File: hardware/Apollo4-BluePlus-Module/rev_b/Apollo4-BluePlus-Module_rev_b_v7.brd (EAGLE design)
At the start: 13 x 20 mm, 102 parts, among them J1 TC2030-JLINK-NL-2SIDE, J2 TC2030-JLINK-NL-2SIDE, P1 CASTELLATION4L, P10 CASTELLATION4L, P11 CASTELLATION4L, P12 CASTELLATION4L, P13 CASTELLATION4L, P14 CASTELLATION4L, P15 CASTELLATION4L, P18 CASTELLATION4L, P19 CASTELLATION4L, P2 CASTELLATION4L, P20 CASTELLATION4L, P21 CASTELLATION4L, P22 CASTELLATION4L, P23 CASTELLATION4L, P24 CASTELLATION4L, P25 CASTELLATION4L, P26 CASTELLATION4L, P27 CASTELLATION4L, P28 CASTELLATION4L, P29 CASTELLATION4L, P3 CASTELLATION4L, P30 CASTELLATION4L, P31 CASTELLATION4L, P32 CASTELLATION4L, P33 CASTELLATION4L, P34 CASTELLATION4L, P35 CASTELLATION4L, P36 CASTELLATION4L, P37 CASTELLATION4L, P38 CASTELLATION4L, P39 CASTELLATION4L, P4 CASTELLATION4L, P40 CASTELLATION4L, P41 CASTELLATION4L, P42 CASTELLATION4L, P43 CASTELLATION4L, P44 CASTELLATION4L, P45 CASTELLATION4L, P46 CASTELLATION4L, P47 CASTELLATION4L, P48 CASTELLATION4L, P5 CASTELLATION4L, P6 CASTELLATION4L, P7 CASTELLATION4L, P8 CASTELLATION4L, P9 CASTELLATION4L, U1 APOLLO4_BLUE_PLUS_SOC_KBR, X1 TXC-9HT12, X2 ABM12W

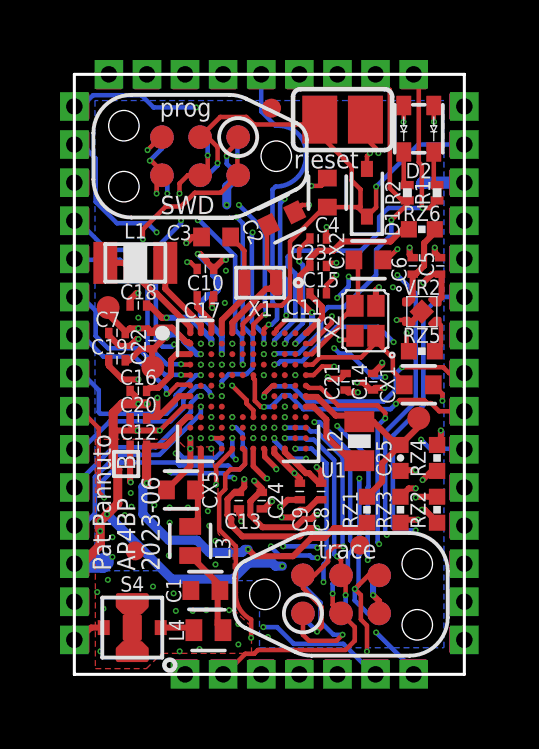
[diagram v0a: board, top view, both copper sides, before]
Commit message: ap4bp-mod-rev_b: remove RF test switch
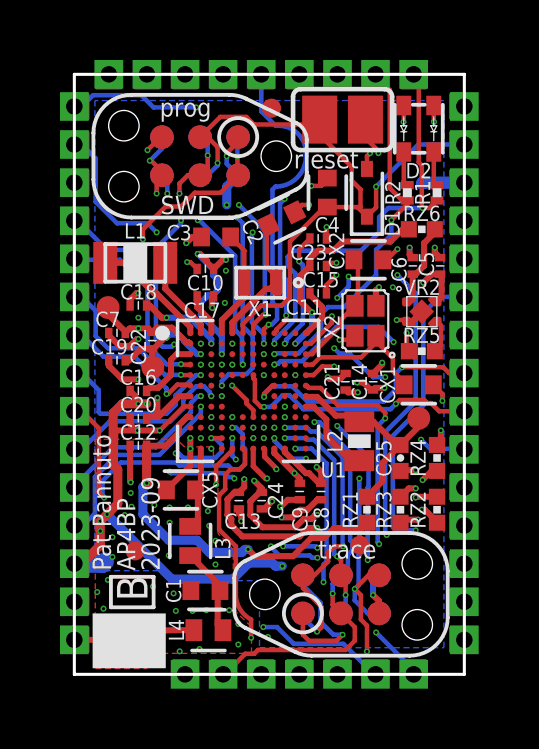
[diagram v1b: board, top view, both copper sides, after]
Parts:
- removed S4: MM8030-2610, switches:MM8030-2610
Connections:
- removed net N$18: L4.2, S4.IN
- net AGND: no longer S4.G1, S4.G2
- net BLE_RFOUT: now also L4.2; no longer S4.OUT
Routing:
- net BLE_RFOUT: track 1.46 -> 4.35 mm
- net N$18: track 1.14 -> 0.00 mm
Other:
- board text added: "2023-09"
- board text removed: "2023-06"
